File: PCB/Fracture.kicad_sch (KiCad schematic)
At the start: 57 parts, among them J1 Conn_01x02, J2 Barrel_Jack, J3 Conn_01x08_Pin, J4 Conn_01x08_Pin, P1 USB_C_Plug, SW1 SW_SPDT, SW2 SW_Push, SW3 SW_Push, U1 AMS1117-3.3, U2 74HC4067PW,118, U3 74HC4067PW,118, U4 AMS1117-3.3, U5 ESP32-S3-WROOM-1-N4, U6 LM2596SX-5.0/NOPB, U7 SP3485EN-L/TR

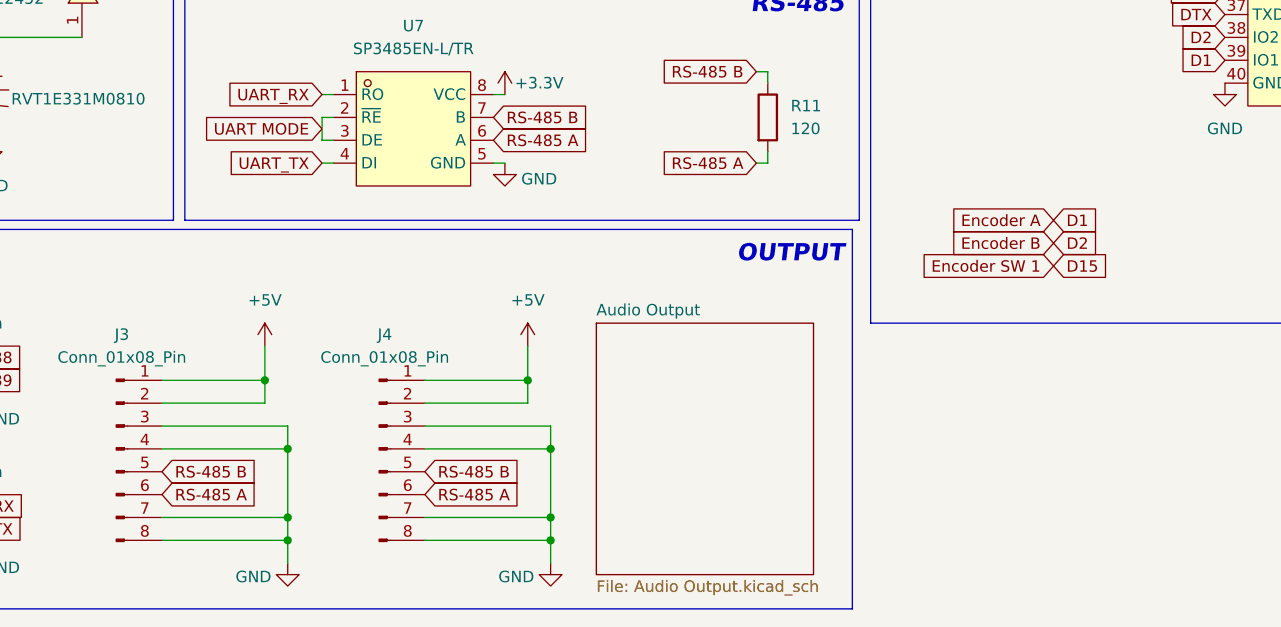
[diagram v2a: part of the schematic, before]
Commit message: Added sensing pins and Schematic Renders
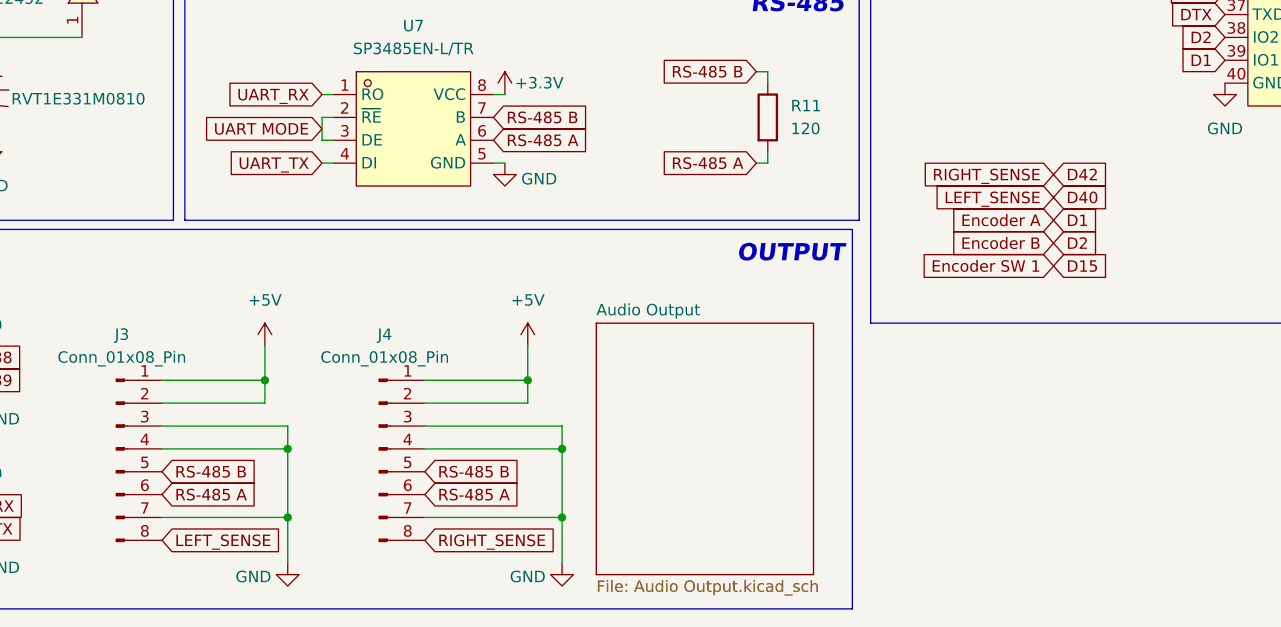
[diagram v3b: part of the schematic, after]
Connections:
- net D40: now also J3.8 (Pin_8)
- net D42: now also J4.8 (Pin_8)
- net GND: no longer J3.8 (Pin_8), J4.8 (Pin_8)
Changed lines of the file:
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@@
 	)
 	(junction
-		(at 142.24 185.42)
+		(at 143.51 185.42)
 		(diameter 0)
 		(color 0 0 0 0)
@@
 	)
 	(junction
-		(at 113.03 187.96)
-		(diameter 0)
-		(color 0 0 0 0)
-	)
-	(junction
 		(at 250.19 31.75)
 		(diameter 0)
@@
 	)
 	(junction
-		(at 142.24 187.96)
-		(diameter 0)
-		(color 0 0 0 0)
-	)
-	(junction
-		(at 142.24 177.8)
+		(at 143.51 177.8)
 		(diameter 0)
 		(color 0 0 0 0)
@@
 	(wire
 		(pts
-			(xy 113.03 190.5) (xy 113.03 187.96)
-		)
-		(stroke
-			(width 0)
-			(type default)
-		)
-	)
-	(wire
-		(pts
 			(xy 85.09 100.33) (xy 83.82 100.33)
 		)
@@
 	(wire
 		(pts
-			(xy 128.27 175.26) (xy 142.24 175.26)
+			(xy 128.27 175.26) (xy 143.51 175.26)
 		)
 		(stroke
@@
 	(wire
 		(pts
-			(xy 142.24 175.26) (xy 142.24 177.8)
+			(xy 143.51 175.26) (xy 143.51 177.8)
 		)
 		(stroke
@@
 	(wire
 		(pts
-			(xy 142.24 190.5) (xy 142.24 187.96)
+			(xy 143.51 185.42) (xy 143.51 190.5)
 		)
 		(stroke
@@
 	(wire
 		(pts
-			(xy 142.24 185.42) (xy 142.24 187.96)
-		)
-		(stroke
-			(width 0)
-			(type default)
-		)
-	)
-	(wire
-		(pts
 			(xy 41.91 144.78) (xy 45.72 144.78)
 		)
@@
 	(wire
 		(pts
-			(xy 113.03 185.42) (xy 113.03 187.96)
+			(xy 113.03 185.42) (xy 113.03 190.5)
 		)
 		(stroke
@@
 	(wire
 		(pts
-			(xy 128.27 185.42) (xy 142.24 185.42)
+			(xy 128.27 185.42) (xy 143.51 185.42)
 		)
 		(stroke
@@
 	(wire
 		(pts
-			(xy 99.06 187.96) (xy 113.03 187.96)
-		)
-		(stroke
-			(width 0)
-			(type default)
-		)
-	)
-	(wire
-		(pts
 			(xy 110.49 46.99) (xy 109.22 46.99)
 		)
@@
 	(wire
 		(pts
-			(xy 142.24 177.8) (xy 128.27 177.8)
+			(xy 143.51 177.8) (xy 128.27 177.8)
 		)
 		(stroke
@@
 	(wire
 		(pts
-			(xy 142.24 185.42) (xy 142.24 177.8)
+			(xy 143.51 185.42) (xy 143.51 177.8)
 		)
 		(stroke
@@
 	(wire
 		(pts
-			(xy 128.27 187.96) (xy 142.24 187.96)
-		)
-		(stroke
-			(width 0)
-			(type default)
-		)
-	)
-	(wire
-		(pts
 			(xy 83.82 62.23) (xy 82.55 62.23)
 		)
@@
 		)
 	)
+	(global_label "D42"
+		(shape input)
+		(at 198.12 147.32 0)
+		(fields_autoplaced yes)
+		(effects
+			(font
+				(size 1.27 1.27)
+			)
+			(justify left)
+		)
+		(property "Intersheetrefs" "${INTERSHEET_REFS}"
+			(at 204.7942 147.32 0)
+			(effects
+				(font
+					(size 1.27 1.27)
+				)
+				(justify left)
+				(hide yes)
+			)
+		)
+	)
 	(global_label "AM1:14"
 		(shape input)
@@
 		)
 	)
+	(global_label "RIGHT_SENSE"
+		(shape input)
+		(at 198.12 147.32 180)
+		(fields_autoplaced yes)
+		(effects
+			(font
+				(size 1.27 1.27)
+			)
+			(justify right)
+		)
+		(property "Intersheetrefs" "${INTERSHEET_REFS}"
+			(at 182.6768 147.32 0)
+			(effects
+				(font
+					(size 1.27 1.27)
+				)
+				(justify right)
+				(hide yes)
+			)
+		)
+	)
 	(global_label "AM1:8"
 		(shape input)
@@
 		)
 	)
+	(global_label "LEFT_SENSE"
+		(shape input)
+		(at 198.12 149.86 180)
+		(fields_autoplaced yes)
+		(effects
+			(font
+				(size 1.27 1.27)
+			)
+			(justify right)
+		)
+		(property "Intersheetrefs" "${INTERSHEET_REFS}"
+			(at 183.8864 149.86 0)
+			(effects
+				(font
+					(size 1.27 1.27)
+				)
+				(justify right)
+				(hide yes)
+			)
+		)
+	)
 	(global_label "D2"
 		(shape input)
@@
 		)
 	)
+	(global_label "D40"
+		(shape input)
+		(at 198.12 149.86 0)
+		(fields_autoplaced yes)
+		(effects
+			(font
+				(size 1.27 1.27)
+			)
+			(justify left)
+		)
+		(property "Intersheetrefs" "${INTERSHEET_REFS}"
+			(at 204.7942 149.86 0)
+			(effects
+				(font
+					(size 1.27 1.27)
+				)
+				(justify left)
+				(hide yes)
+			)
+		)
+	)
 	(global_label "DTX"
 		(shape input)
@@
 		)
 	)
+	(global_label "RIGHT_SENSE"
+		(shape input)
+		(at 128.27 187.96 0)
+		(fields_autoplaced yes)
+		(effects
+			(font
+				(size 1.27 1.27)
+			)
+			(justify left)
+		)
+		(property "Intersheetrefs" "${INTERSHEET_REFS}"
+			(at 143.7132 187.96 0)
+			(effects
+				(font
+					(size 1.27 1.27)
+				)
+				(justify left)
+				(hide yes)
+			)
+		)
+	)
 	(global_label "LED_DATA"
 		(shape input)
@@
 		)
 	)
+	(global_label "LEFT_SENSE"
+		(shape input)
+		(at 99.06 187.96 0)
+		(fields_autoplaced yes)
+		(effects
+			(font
+				(size 1.27 1.27)
+			)
+			(justify left)
+		)
+		(property "Intersheetrefs" "${INTERSHEET_REFS}"
+			(at 113.2936 187.96 0)
+			(effects
+				(font
+					(size 1.27 1.27)
+				)
+				(justify left)
+				(hide yes)
+			)
+		)
+	)
 	(global_label "D37"
 		(shape input)
@@
 	(symbol
 		(lib_id "power:GND")
-		(at 142.24 190.5 0)
+		(at 143.51 190.5 0)
 		(unit 1)
 		(exclude_from_sim no)
@@
 		(dnp no)
 		(property "Reference" "#PWR059"
-			(at 142.24 196.85 0)
+			(at 143.51 196.85 0)
 			(effects
 				(font
@@
 		)
 		(property "Value" "GND"
-			(at 138.43 192.024 0)
+			(at 139.7 192.024 0)
 			(effects
 				(font
@@
 		)
 		(property "Footprint" ""
-			(at 142.24 190.5 0)
+			(at 143.51 190.5 0)
 			(effects
 				(font
@@
 		)
 		(property "Datasheet" ""
-			(at 142.24 190.5 0)
+			(at 143.51 190.5 0)
 			(effects
 				(font
@@
 		)
 		(property "Description" "Power symbol creates a global label with name \"GND\" , ground"
-			(at 142.24 190.5 0)
+			(at 143.51 190.5 0)
 			(effects
 				(font
